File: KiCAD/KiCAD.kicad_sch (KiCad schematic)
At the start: 0 parts

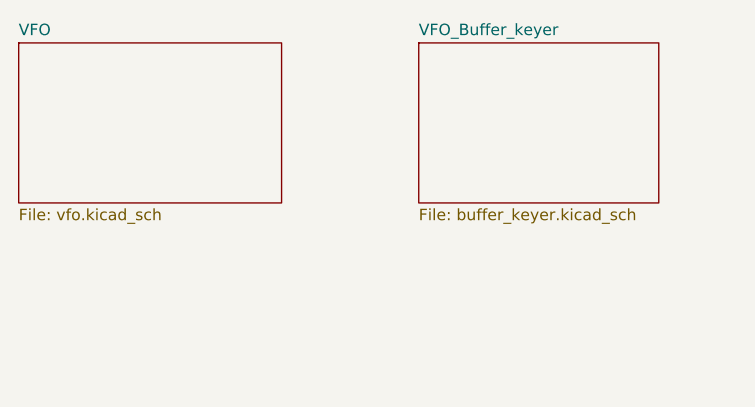
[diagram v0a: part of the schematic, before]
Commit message: kicad: control-board sheets — buffer_keyer keyer body, arduino SPI labels, custom-symbol plan
- buffer_keyer.kicad_sch: place MC1496 keyer support components
  (carrier divider R11/R12, modulator port R3, emitter-degen Re,
  modulator coupling C1, VEE bypass C5, R2 Iee, bypass network),
  MCP4921 envelope DAC U4 with reconstruction cap C3, terminal
  blocks J1/J2/J3 for +5V/+12V/-90V/VEE input, hierarchical labels
  for VFO_OUT, SCK, MOSI, CS_DAC.
- arduino.kicad_sch: add SCK and MOSI hierarchical outputs for SPI
  link to MCP4921. CS_DAC still TODO.
- vfo.kicad_sch + KiCAD.kicad_sch: minor edits, sheet pin updates.
- Documentation/kicad_custom_symbols.md: new doc — pattern and plan
  for project-local xmitter:Metro_ESP32S3 symbol to replace the
  cluttered stock symbol (~30 pins → 10 pins, project-named).
- VFO_Keyer_Order.xlsx: small status updates.
- xmitter_prj/keyer.sch: minor cleanup.
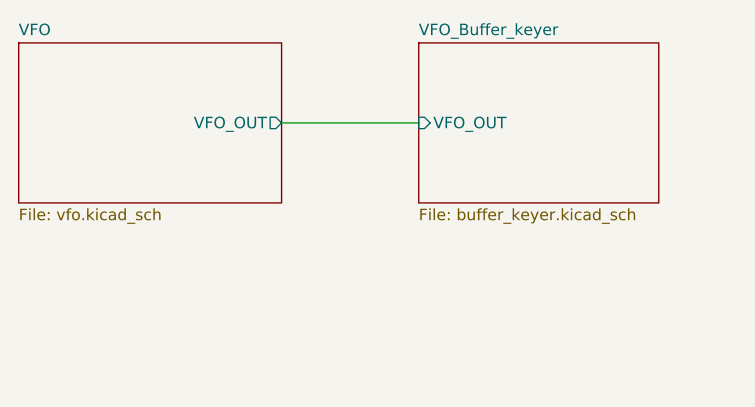
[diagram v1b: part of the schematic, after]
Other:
- sheet VFO ports: added VFO_OUT; removed none
- sheet VFO_Buffer_keyer ports: added VFO_OUT; removed none
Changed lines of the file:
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@@
 	(generator_version "10.0")
 	(paper "A4")
+	(wire
+		(pts
+			(xy 59.69 50.8) (xy 74.93 50.8)
+		)
+		(stroke
+			(width 0)
+			(type default)
+		)
+	)
 	(sheet
 		(at 90.17 106.68)
@@
 			)
 		)
+		(pin "VFO_OUT" input
+			(at 74.93 50.8 180)
+			(effects
+				(font
+					(size 1.27 1.27)
+				)
+				(justify left)
+			)
+		)
 		(instances
 			(project "KiCAD"
@@
 			)
 		)
+		(pin "VFO_OUT" output
+			(at 59.69 50.8 0)
+			(effects
+				(font
+					(size 1.27 1.27)
+				)
+				(justify right)
+			)
+		)

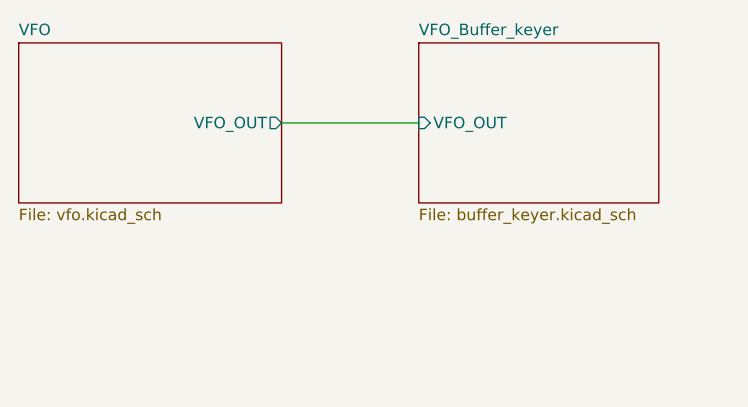
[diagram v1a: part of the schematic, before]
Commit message: kicad: rename VFO_OUT signals to direction-named labels (RAW_RF_*, MOD_RF_*)
The 14 MHz unmodulated signal between VFO and buffer_keyer was
labeled "VFO_OUT" on BOTH sheets, which was directionally ambiguous.
The differential post-modulation outputs of the LM7171 stage were
also labeled "VFO_OUT+/-", which was wrong — by that point in the
chain the signal is keyed/modulated, not raw VFO.

Renames:
- vfo.kicad_sch: hier label VFO_OUT (output) -> RAW_RF_OUT
- buffer_keyer.kicad_sch: hier label VFO_OUT (input) -> RAW_RF_IN
- buffer_keyer.kicad_sch: VFO_OUT+ (output) -> MOD_RF_OUT+
- buffer_keyer.kicad_sch: VFO_OUT- (output) -> MOD_RF_OUT- (also fixed
  a typo where the minus side was mistakenly named MOD_RF-OUT- with a
  hyphen between RF and OUT)
- KiCAD.kicad_sch (root): two sheet pins renamed to match
  (VFO sheet -> RAW_RF_OUT; VFO_Buffer_keyer sheet -> RAW_RF_IN). Pin
  coordinates and UUIDs preserved so existing root-sheet wiring stays
  attached.

Also added Documentation/Components/lm7171.pdf (TI datasheet) - was
already referenced in the supply-voltage compliance audit but hadn't
been committed.
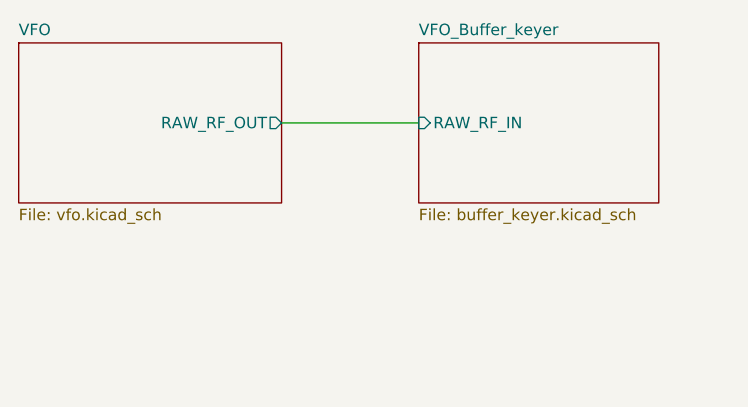
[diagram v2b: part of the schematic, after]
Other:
- sheet VFO ports: added RAW_RF_OUT; removed VFO_OUT
- sheet VFO_Buffer_keyer ports: added RAW_RF_IN; removed VFO_OUT
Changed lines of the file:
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@@
 			)
 		)
-		(pin "VFO_OUT" input
+		(pin "RAW_RF_IN" input
 			(at 74.93 50.8 180)
 			(effects
@@
 			)
 		)
-		(pin "VFO_OUT" output
+		(pin "RAW_RF_OUT" output
 			(at 59.69 50.8 0)
 			(effects
